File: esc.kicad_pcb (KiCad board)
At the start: 4 copper layers, 67 x 114.5 mm, 73 parts, among them J1 Conn_01x02, J2 Screw_Terminal_01x01, J3 Screw_Terminal_01x01, J4 Screw_Terminal_01x01, J5 3220-10-0100-00, Q1 SIR182DP-T1-RE3, Q2 SIR182DP-T1-RE3, Q3 SIR182DP-T1-RE3, Q4 SIR182DP-T1-RE3, Q5 SIR182DP-T1-RE3, Q6 SIR182DP-T1-RE3, SW1 RotaryEncoder, U1 TPS7A20xxxDQN, U2 STM32G484CETx, U3 TPS562201DDCR, U4 TVS0500DRV, U5 IR2103STRPBF, U6 IR2103STRPBF, U7 IR2103STRPBF, Y1 32.768KHz

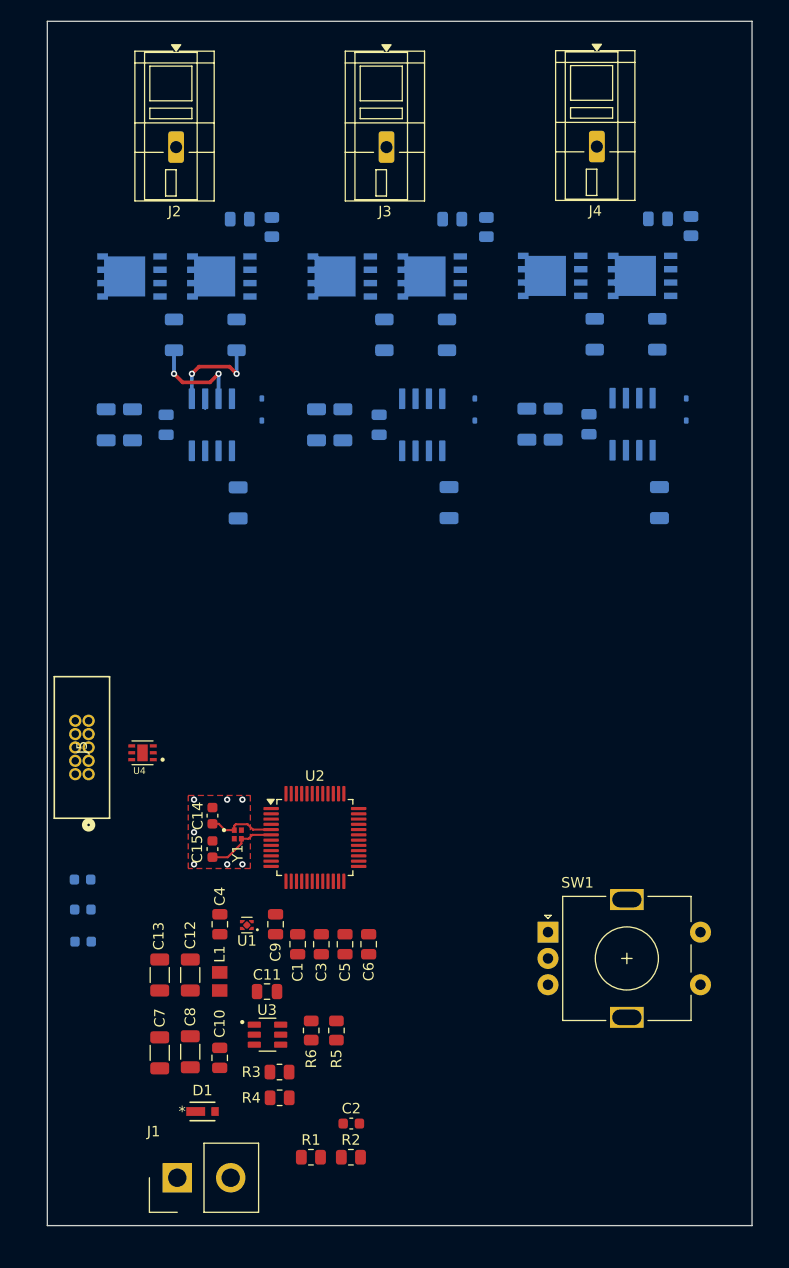
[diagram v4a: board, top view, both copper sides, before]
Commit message: PDN complete
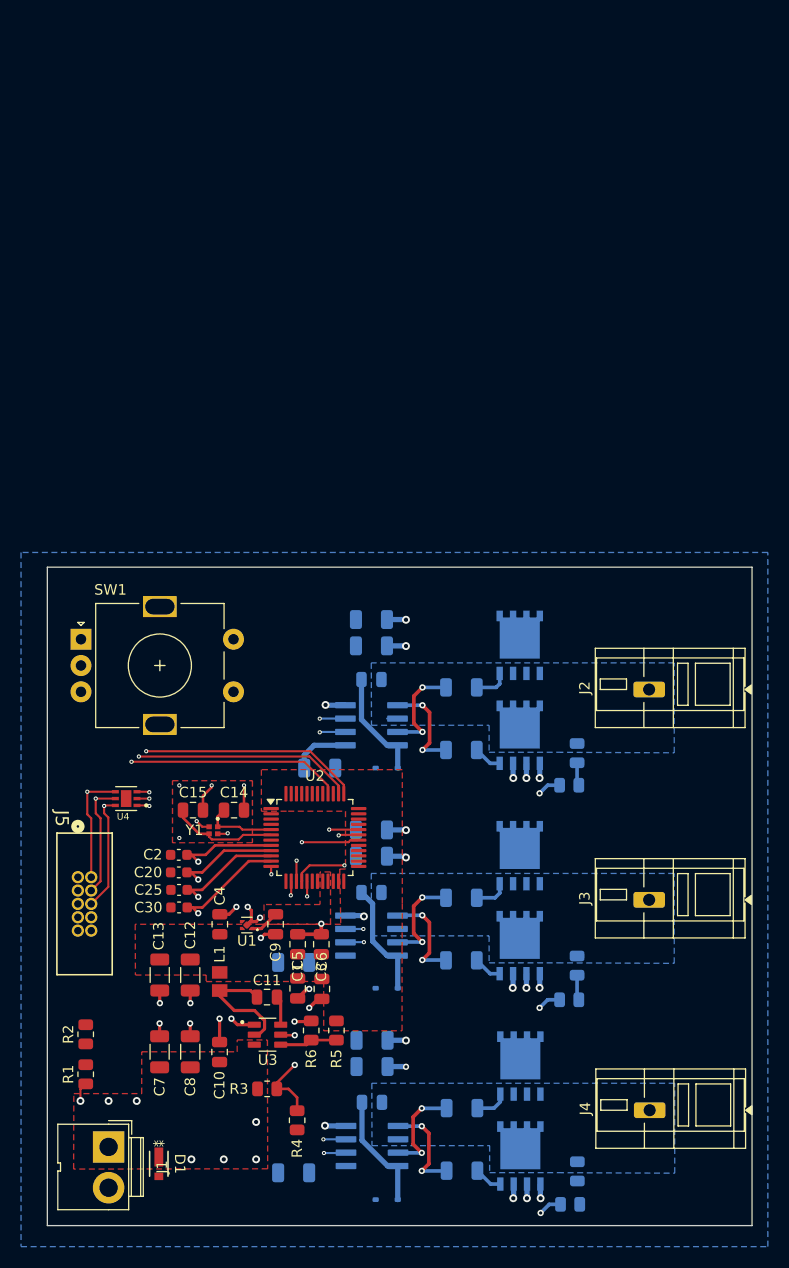
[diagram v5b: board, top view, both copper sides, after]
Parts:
- C14, C15: footprint Capacitor_SMD:C_0603_1608Metric -> Capacitor_SMD:C_0805_2012Metric
- C20, C25, C30: moved to F.Cu
- J1: footprint Connector_Samtec_HPM_THT:Samtec_HPM-02-01-x-S_Straight_1x02_Pitch5.08mm -> Connector:JWT_A3963_1x02_P3.96mm_Vertical
- moved R18 93.7 mm to (142.2, 173.0), turned to 180 degrees
- moved J4 91.8 mm to (149.8, 164.0), turned to 90 degrees
- moved R17 90.9 mm to (142.9, 169.8), turned to -90 degrees
- moved Q6 84.5 mm to (137.5, 168.4), turned to 90 degrees
- moved R16 81.7 mm to (131.9, 169.8), turned to 180 degrees
- moved D4 80.3 mm to (124.8, 172.5), turned to 180 degrees
- moved J3 75.8 mm to (149.7, 144.0), turned to 90 degrees
- moved Q5 75.2 mm to (137.5, 159.8), turned to 90 degrees
- moved R15 74.6 mm to (131.9, 163.8), turned to 180 degrees
- moved R14 73.9 mm to (142.1, 153.5), turned to 180 degrees
- moved U7 73.0 mm to (123.4, 167.4), turned to 0 degrees
- moved C26 72.6 mm to (115.9, 170.0), turned to 180 degrees
- moved R13 72.0 mm to (142.9, 150.3), turned to -90 degrees
- moved J2 68.4 mm to (149.7, 124.0), turned to 90 degrees
- moved C27 67.7 mm to (123.4, 163.3), turned to 0 degrees
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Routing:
- net GND: track 0.07 -> 70.5 mm, vias 7 -> 44
- net /STM32/SWDIO: track 0.00 -> 40.1 mm, vias 0 -> 2
- net /STM32/SWCLK: track 0.00 -> 39.3 mm, vias 0 -> 2
- net /STM32/SWO: track 0.00 -> 37.6 mm, vias 0 -> 2
- net /STM32/W_HIN: track 0.00 -> 37.2 mm, vias 0 -> 2
- net /STM32/ENC_B: track 0.00 -> 36.1 mm, vias 0 -> 1
- net /STM32/ENC_A: track 0.00 -> 35.0 mm, vias 0 -> 1
- net /STM32/W_LIN: track 0.00 -> 29.2 mm, vias 0 -> 2
- net /STM32/U_HIN: track 0.00 -> 19.2 mm, vias 0 -> 2
- net /STM32/U_LIN: track 0.00 -> 18.8 mm, vias 0 -> 2
- net /STM32/V_HIN: track 0.00 -> 14.8 mm, vias 0 -> 2
- net /STM32/V_LIN: track 0.00 -> 13.7 mm, vias 0 -> 2
- net /STM32/V_VSENSE: track 0.00 -> 13.0 mm, vias 0 -> 1
- net /STM32/U_VSENSE: track 0.00 -> 12.4 mm, vias 0 -> 1
- net /PWR/BST: track 0.00 -> 11.6 mm
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- added copper zone on F.Cu, net +3V3
- added copper zone on B.Cu, net /U PHASE/U_PHASE
- added copper zone on B.Cu, net /V PHASE/V_PHASE
- added copper zone on B.Cu, net /W PHASE/W_PHASE
- added copper zone on In1.Cu, net GND
- added copper zone on In2.Cu, net GND
- added copper zone on B.Cu, net VCC
- added copper zone on F.Cu, net VCC
- added copper zone on F.Cu, net VDDA
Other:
- board size 67 x 114.5 mm -> 67 x 62.6 mm

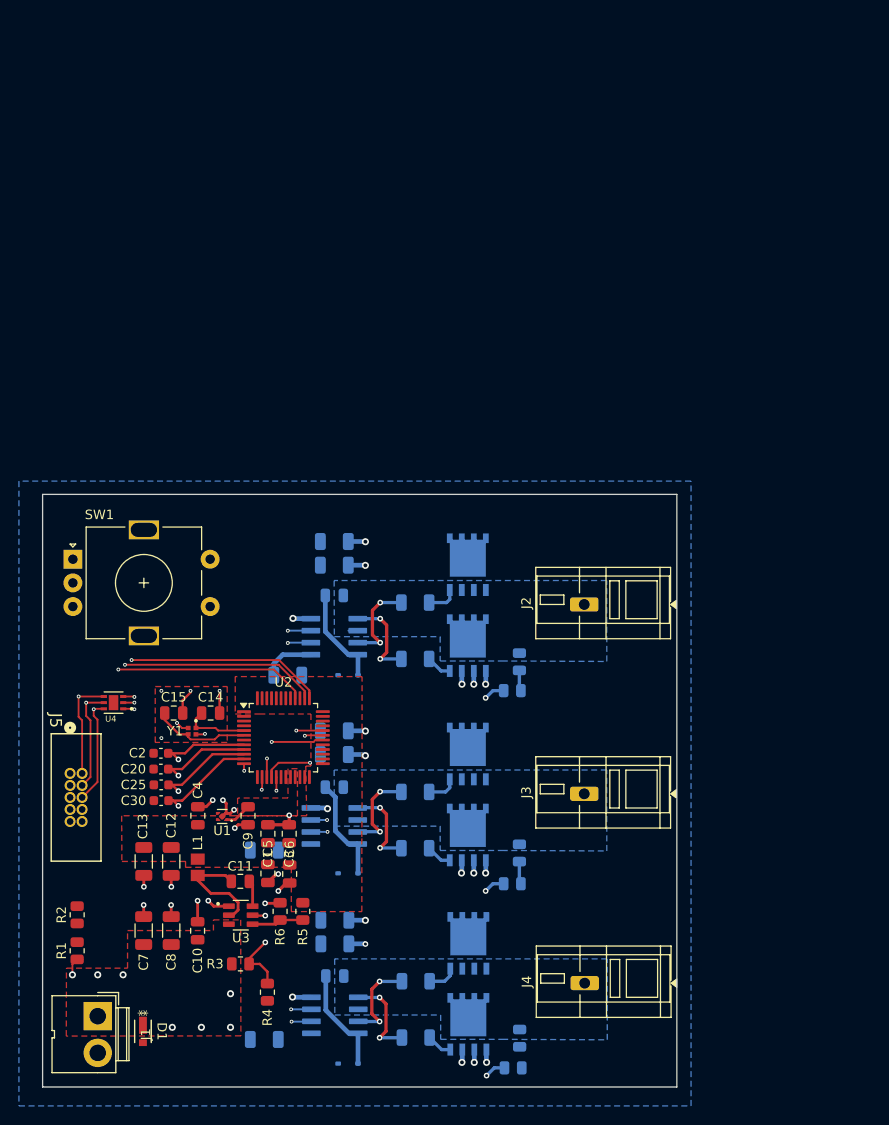
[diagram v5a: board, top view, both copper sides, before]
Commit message: completed layout -- DRC
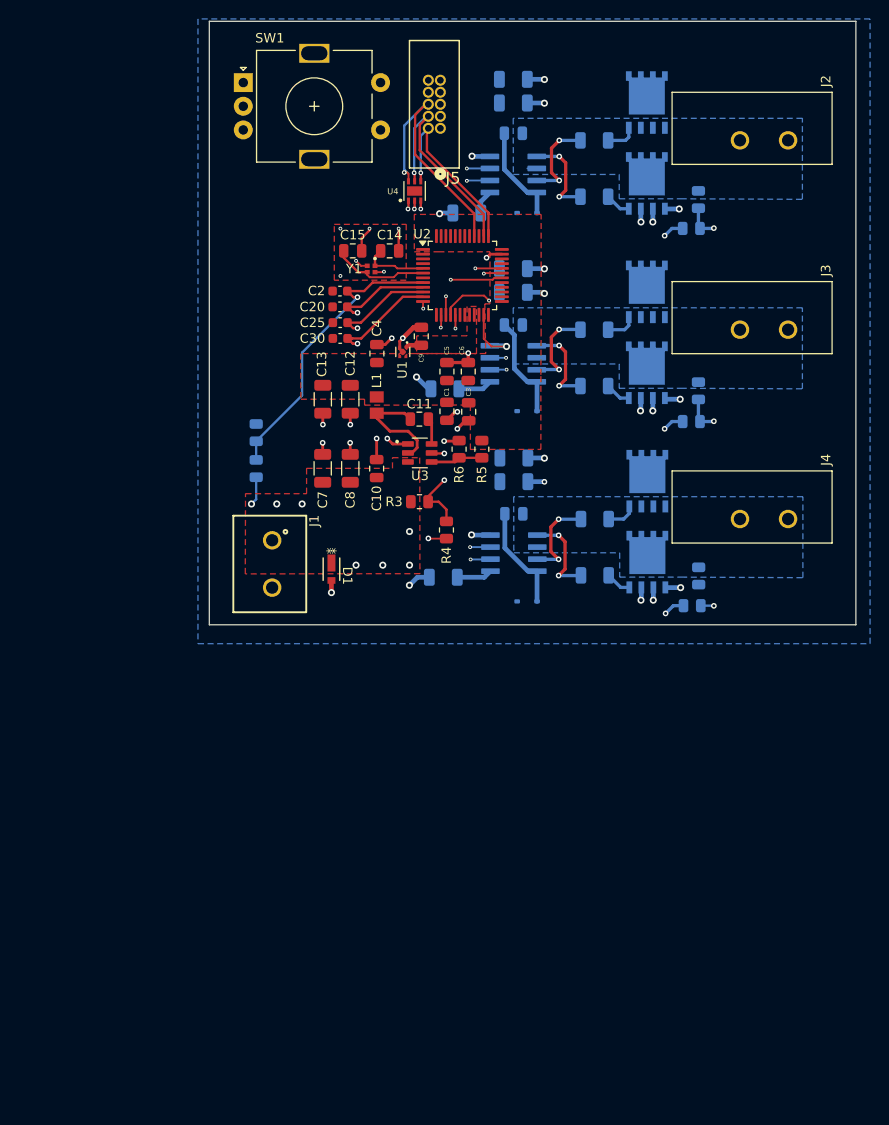
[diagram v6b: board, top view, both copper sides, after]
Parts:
- J1: footprint Connector:JWT_A3963_1x02_P3.96mm_Vertical -> esc-land-patterns:691137710002
- J2, J3, J4: footprint TerminalBlock_WAGO:TerminalBlock_WAGO_236-101_1x01_P5.00mm_45Degree -> esc-land-patterns:PHOENIX_1706701
- R1, R2: moved to B.Cu
- moved J5 78.6 mm to (134.5, 73.7), turned to 90 degrees
- moved U4 62.7 mm to (131.8, 80.3), turned to 90 degrees
- moved R1 54.3 mm to (115.1, 109.7)
- moved R2 54.3 mm to (115.1, 105.9)
- moved C9 53.9 mm to (132.5, 95.7), turned to 90 degrees
- moved SW1 53.5 mm to (113.7, 68.9)
- moved J2 53.4 mm to (175.9, 77.5)
- moved J3 53.4 mm to (175.9, 97.5)
- moved J4 53.3 mm to (175.9, 117.5)
- moved D1 52.7 mm to (123.0, 120.3)
- moved U1 52.7 mm to (130.6, 97.3), turned to -90 degrees
- moved Q3 52.4 mm to (156.3, 91.0)
- moved C12 52.4 mm to (125.0, 102.3)
- moved C13 52.4 mm to (122.1, 102.3)
- moved C22 52.4 mm to (142.2, 94.5)
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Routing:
- net /STM32/W_VSENSE: track 11.1 -> 83.4 mm, vias 1 -> 2
- net /STM32/U_VSENSE: track 12.4 -> 57.8 mm, vias 1 -> 2
- net /STM32/V_VSENSE: track 13.0 -> 56.2 mm, vias 1 -> 2
- net /PWR/VCC_SENSE: track 9.72 -> 31.8 mm
- net /STM32/SWDIO: track 40.1 -> 20.1 mm, vias 2 -> 1
- net GND: track 70.5 -> 85.9 mm, vias 44 -> 48
- net /STM32/SWCLK: track 39.3 -> 24.7 mm, vias 2 -> 1
- net /STM32/SWO: track 37.6 -> 27.2 mm, vias 2 -> 1
- net VCC: track 7.94 -> 13.0 mm
- net /STM32/ENC_A: track 35.0 -> 38.4 mm
- net VDDA: track 2.85 -> 1.53 mm
- net /STM32/ENC_B: track 36.1 -> 37.2 mm
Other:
- board size 67 x 62.6 mm -> 68.3 x 63.8 mm

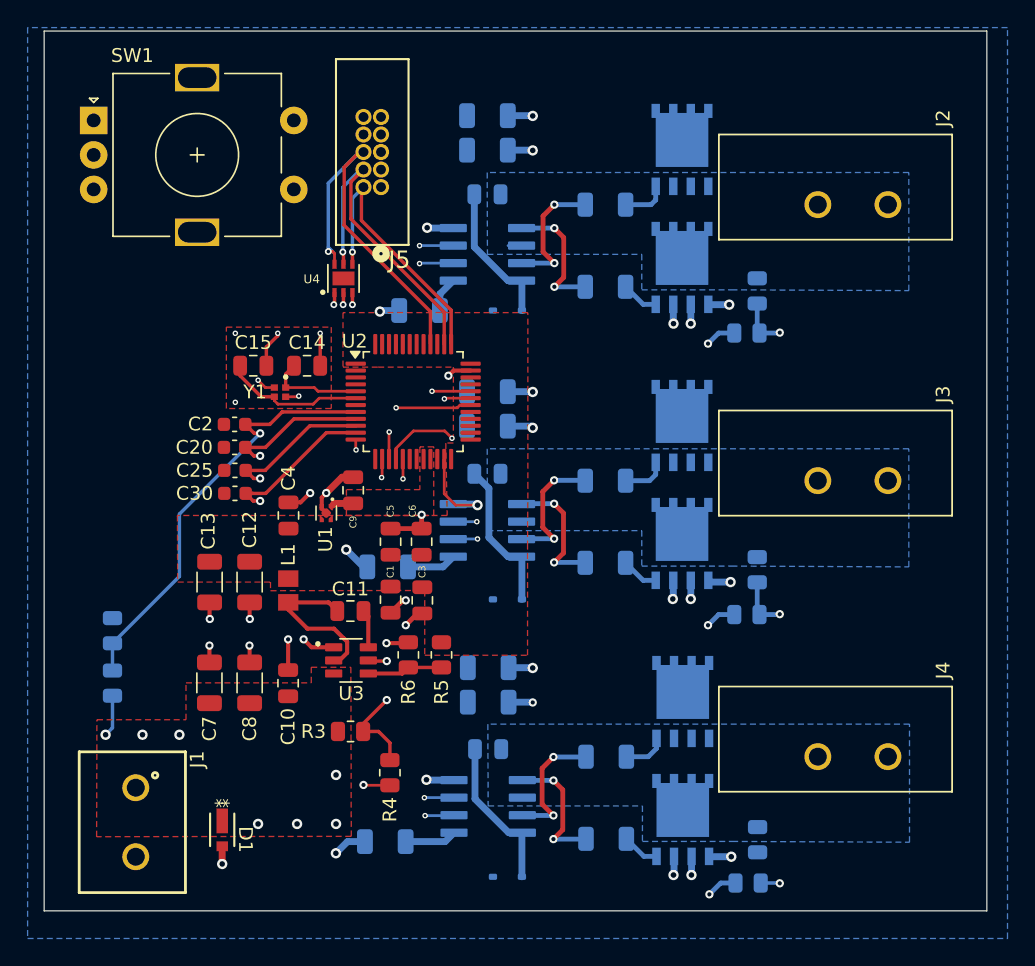
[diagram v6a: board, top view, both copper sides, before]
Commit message: cleaning up routing
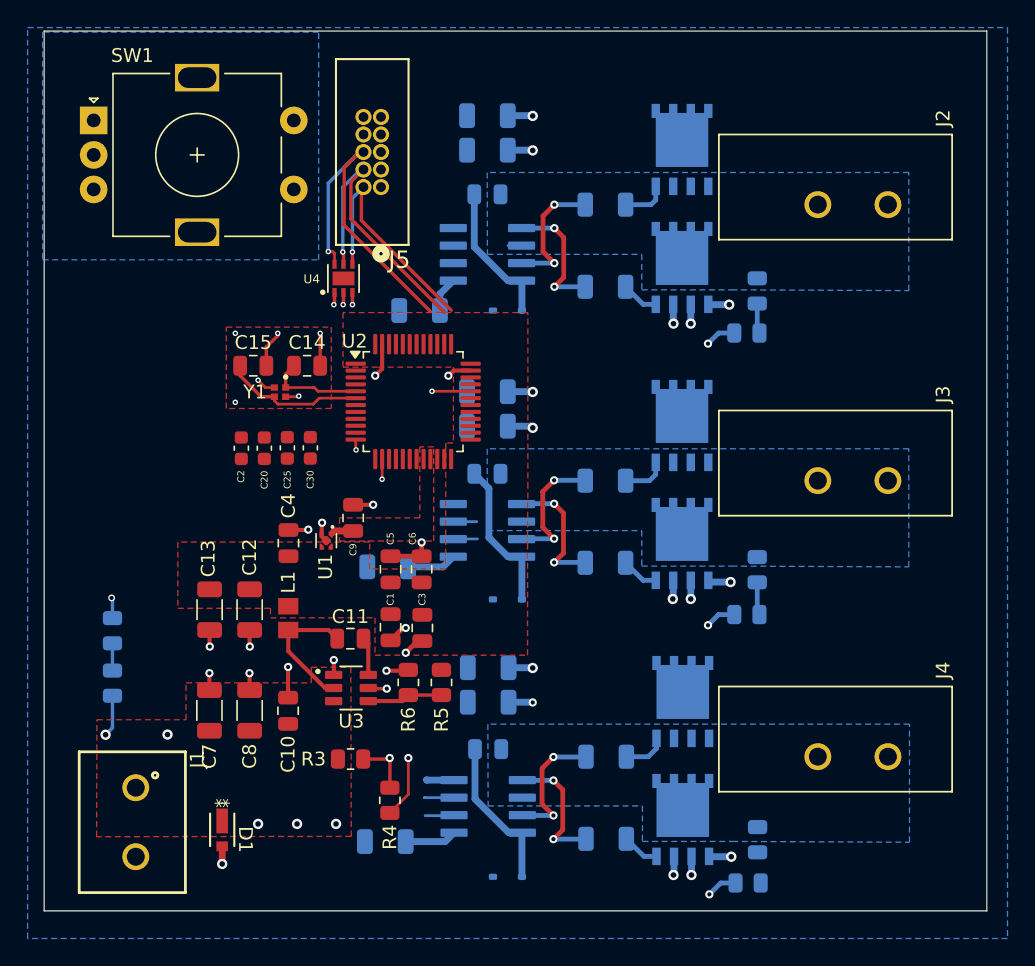
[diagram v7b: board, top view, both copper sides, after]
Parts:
- moved C30 6.38 mm to (129.4, 92.6), turned to -90 degrees
- moved C25 4.13 mm to (127.7, 92.6), turned to -90 degrees
- moved C20 2.15 mm to (126.1, 92.7), turned to -90 degrees
- moved C1 2.00 mm to (135.2, 101.4)
- moved C10 2.00 mm to (127.8, 111.7)
- moved C11 2.00 mm to (132.3, 106.5)
- moved C12 2.00 mm to (125.0, 104.3)
- moved C13 2.00 mm to (122.1, 104.3)
- moved C3 2.00 mm to (137.5, 101.4)
- moved C4 2.00 mm to (127.8, 99.5)
- moved C5 2.00 mm to (135.2, 105.6)
- moved C6 2.00 mm to (137.5, 105.7)
- moved C7 2.00 mm to (122.1, 111.7)
- moved C8 2.00 mm to (125.0, 111.7)
- moved C9 2.00 mm to (132.5, 97.7)
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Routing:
- net /STM32/W_VSENSE: track 83.4 -> 0.00 mm, vias 2 -> 0
- net /STM32/U_VSENSE: track 57.8 -> 2.20 mm, vias 2 -> 0
- net /STM32/V_VSENSE: track 56.2 -> 2.40 mm, vias 2 -> 0
- net /PWR/VCC_SENSE: track 31.8 -> 1.98 mm, vias 1 -> 0
- net /STM32/U_HIN: track 19.2 -> 0.00 mm, vias 2 -> 0
- net /STM32/U_LIN: track 18.8 -> 0.00 mm, vias 2 -> 0
- net /STM32/V_HIN: track 14.8 -> 1.76 mm, vias 2 -> 0
- net GND: track 85.9 -> 74.6 mm, vias 48 -> 45
- net /STM32/V_LIN: track 14.2 -> 8.57 mm, vias 2 -> 0
- net /STM32/SWO: track 27.2 -> 24.6 mm
- net /STM32/SWDIO: track 20.1 -> 17.6 mm
- net /STM32/SWCLK: track 24.7 -> 22.4 mm
- net /PWR/BST: track 11.6 -> 9.81 mm
- net /STM32/W_LIN: track 29.2 -> 27.8 mm, vias 2 -> 0
- net VCC: vias 7 -> 5
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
